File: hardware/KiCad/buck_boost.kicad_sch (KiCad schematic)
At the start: 51 parts, among them Q1 BSC030N08NS5, Q2 BSC030N08NS5, Q3 BSC030N08NS5, Q4 BSC030N08NS5, U2 CC6937S8-3FB020, U3 CC6937S8-3FB020

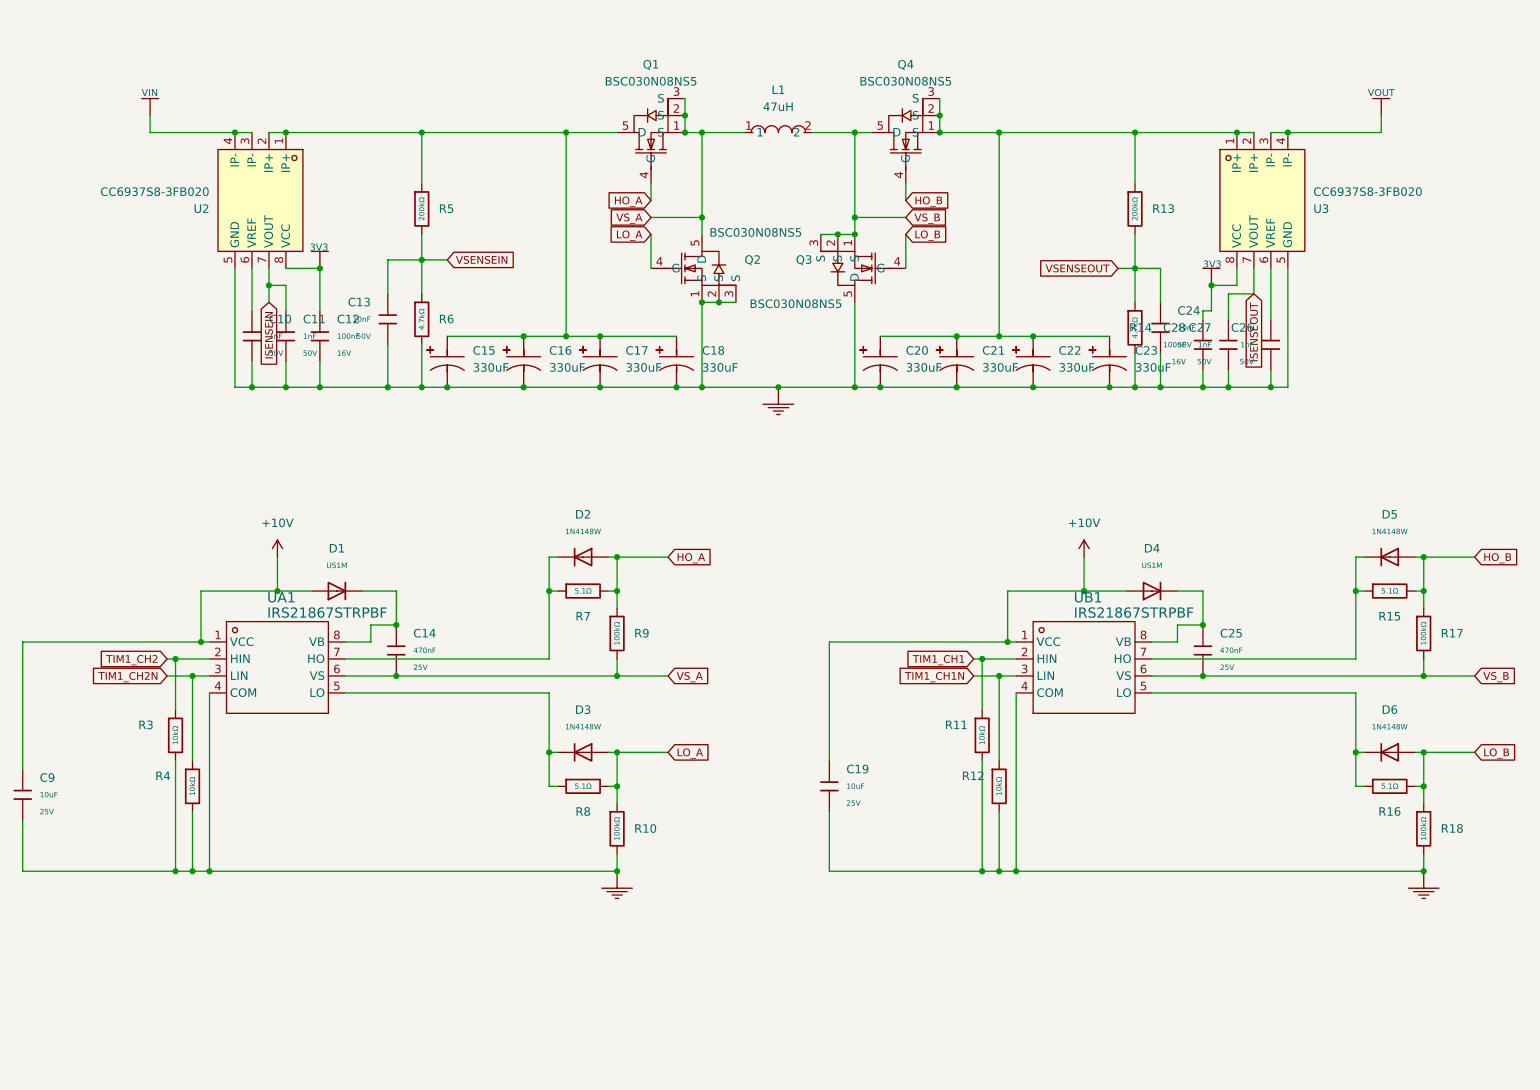
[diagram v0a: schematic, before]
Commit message: Vendor easyeda2kicad component library; rename project files; fix stale part data
Vendors the 16 easyeda2kicad:* parts (symbols/footprints/3D models) that
were referenced but never committed, registers them in sym-lib-table and
a new fp-lib-table, and adds the EASYEDA2KICAD project text variable so
existing 3D-model paths resolve.

Also corrects BSC030N08NS5's stale metadata (was pointing at an ElecSuper
clone, C49108769, instead of the genuine Infineon part, C501507) and
swaps its footprint to the freshly-fetched one, and fixes STANDARDS.md's
Hardware Universe table (stale reference designators, stale MOSFET/
CC6937 LCSC numbers, ~13 previously undocumented parts, wrong library
path).

Renames the auto-generated project/sheet filenames to something legible:
ProPrj_STM32 MPPT_2024-07-25_15-40-35_2026-05-30.* -> openMPPT_v1.3.*,
and the numbered "N_Name Stuff.kicad_sch" sheets -> mcu/buck_boost/
connectors.kicad_sch. Verified via kicad-cli ERC/DRC before and after -
same violation counts, no structural breakage.

Co-Authored-By: Claude Sonnet 5 <noreply@anthropic.com>
Claude-Session: https://claude.ai/code/session_01FKwww6crXDCSrRUFRETJEs
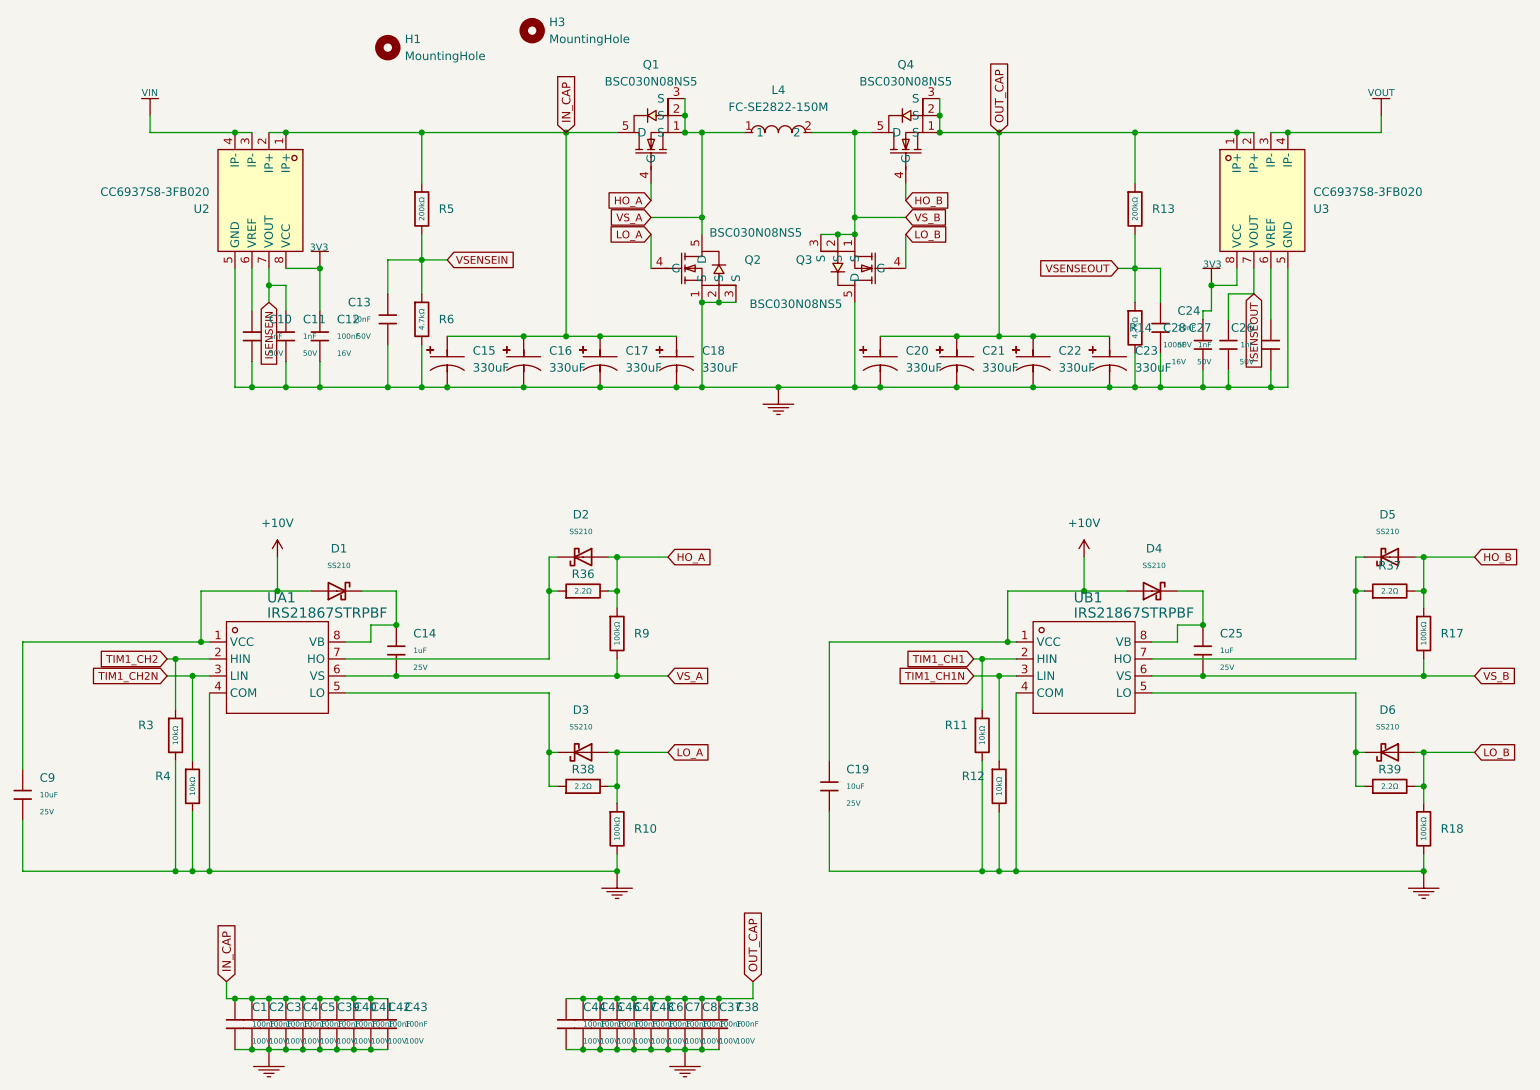
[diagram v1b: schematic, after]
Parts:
- removed C14, C25: 470nF, PCM_JLCPCB:C_0603, symbol JLCPCB-Capacitors:0603,470nF
- removed D1, D4: US1M, PCM_JLCPCB:D_SMA, symbol JLCPCB-Diodes:Recovery,US1M
- removed D2, D3, D5, D6: 1N4148W, PCM_JLCPCB:D_SOD-123, symbol JLCPCB-Diodes:Switching,1N4148W,(2)
- removed L1: 47uH, easyeda2kicad:IND-TH_L32.2-W22.2_CPEX3222L, symbol easyeda2kicad:CPEX3222L-470MC-RS
- removed R15, R16, R7, R8: 5.1Ω, PCM_JLCPCB:R_0603, symbol JLCPCB-Resistors:0603,5.1Ω
- added C1, C2, C3, C37, C38, C39, C4, C40, C41, C42, C43, C44, C45, C46, C47, C48, C5, C6, C7, C8: 100nF, PCM_JLCPCB:C_0805, symbol JLCPCB-Capacitors:0805,100nF
- added C14, C25: 1uF, PCM_JLCPCB:C_0402, symbol JLCPCB-Capacitors:0402,1uF
- added D1, D2, D3, D4, D5, D6: SS210, PCM_JLCPCB:D_SMA, symbol JLCPCB-Diodes:Schottky,SS210
- added H1, H3: MountingHole, MountingHole:MountingHole_3.2mm_M3_DIN965, symbol Mechanical:MountingHole
- added L4: FC-SE2822-150M, easyeda2kicad:IND-TH_L28.0-W23.0_FC-SE2822, symbol easyeda2kicad:FC-SE2822-150M
- added R36, R37, R38, R39: 2.2Ω, PCM_JLCPCB:R_0603, symbol JLCPCB-Resistors:0603,2.2Ω
- Q1, Q2, Q3, Q4: footprint easyeda2kicad:TDSON-8_L5.9-W5.2-P1.27-BL-1 -> easyeda2kicad:PG-TDSON-8_L5.0-W6.0-P1.27-BL-EP; LCSC Part C49108769 -> C501507; MPN BSC030N08NS5(ES) -> BSC030N08NS5; Manufacturer ElecSuper(静芯) -> Infineon
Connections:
- net +10V: now also D1.2, D4.2
- net GND: now also C1.2, C2.2, C3.2, C37.2, C38.2, C39.2, C4.2, C40.2, C41.2, C42.2, C43.2, C44.2, C45.2, C46.2, C47.2, C48.2, C5.2, C6.2, C7.2, C8.2
- net HO_A: now also D2.2, R36.2
- net HO_B: now also D5.2, R37.2
- net LO_A: now also D3.2, R38.2
- net LO_B: now also D6.2, R39.2
- net VS_A: now also C14.2, L4.1
- net VS_B: now also C25.2, L4.2
- net IN_CAP: now reaches C15.1 (+), C16.1 (+), C17.1 (+), C18.1 (+), Q1.5 (D), R5.1, U2.1 (IP+), U2.2 (IP+)
- net IN_CAP: now also C1.1, C2.1, C3.1, C39.1, C4.1, C40.1, C41.1, C42.1, C43.1, C5.1
- net at UA1.7 (HO): now also D2.1, R36.1
- net at UA1.5 (LO): now also D3.1, R38.1
- net at UB1.5 (LO): now also D6.1, R39.1
- net at UA1.8 (VB): now also C14.1, D1.1
- net OUT_CAP: now reaches C20.1 (+), C21.1 (+), C22.1 (+), C23.1 (+), Q4.1 (S), Q4.2 (S), Q4.3 (S), R13.1, U3.1 (IP+), U3.2 (IP+)
- net OUT_CAP: now also C37.1, C38.1, C44.1, C45.1, C46.1, C47.1, C48.1, C6.1, C7.1, C8.1
- net at UB1.7 (HO): now also D5.1, R37.1
- net at UB1.8 (VB): now also C25.1, D4.1

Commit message: fix: correct diode part data, select L4 inductor, drop DRC/ERC mandate
Diode inventory (D1-D7): replaced STANDARDS.md's fictional D_BOOT (US1M)
and D_OFF (1N4148W) rows - never actually placed - with the real,
schematic-verified parts: SS210 for both the gate-driver bootstrap role
(D1/D4) and gate-discharge role (D2/D3/D5/D6), and SS510 as the SCT2A25
switch-node freewheeling diode (D7). Fixes the PCB footprint mismatch on
D2/D3/D5/D6 (D_SOD-123 -> D_SMA, matching what the schematic already
specified and SS210 actually needs) and the JLCPCB/PCM_JLCPCB library
nickname mismatch on UA1/UB1's footprint reference.

L4 main inductor: replaced FC-SE2822-150M with HCZH-3218-150-M (C53699952)
in the schematic - same 15uH, lower DCR (3.5mOhm -> 2.2mOhm, cutting
conduction loss from 1.40W to 0.88W) for a $1.56 premium. Chosen after
evaluating and rejecting a higher-margin option (RSEQ32-220M) that cost
2.7x more and had far less stock for headroom this design doesn't need.
Full reasoning and rejected alternatives documented in CALCULATIONS.typ
Section 8. PCB footprint not yet updated for L4 (different pad format,
needs a deliberate swap, not a drop-in edit).

DRC/ERC: removed the "Claude runs kicad-cli DRC/ERC" mandate from
STANDARDS.md - board correctness review is the user's job, not something
to check automatically or by default.

Co-Authored-By: Claude Sonnet 5 <noreply@anthropic.com>
Claude-Session: https://claude.ai/code/session_01FKwww6crXDCSrRUFRETJEs
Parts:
- L4: value FC-SE2822-150M -> HCZH-3218-150-M; footprint easyeda2kicad:IND-TH_L28.0-W23.0_FC-SE2822 -> easyeda2kicad:IND-TH_L33.5-W23.0-P12.00_HCZH-3218; symbol easyeda2kicad:FC-SE2822-150M -> easyeda2kicad:HCZH-3218-150-M; LCSC Part C46553544 -> C53699952; MPN FC-SE2822-150M -> HCZH-3218-150-M; Manufacturer FC(方成) -> YOUCHI(佑驰)
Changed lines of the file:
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@@
 	)
 	(symbol
-		(lib_id "easyeda2kicad:FC-SE2822-150M")
+		(lib_id "easyeda2kicad:HCZH-3218-150-M")
 		(at 144.78 43.18 0)
 		(unit 1)
@@
 			)
 		)
-		(property "Value" "FC-SE2822-150M"
+		(property "Value" "HCZH-3218-150-M"
 			(at 144.78 39.37 0)
 			(show_name no)
@@
 			)
 		)
-		(property "Footprint" "easyeda2kicad:IND-TH_L28.0-W23.0_FC-SE2822"
+		(property "Footprint" "easyeda2kicad:IND-TH_L33.5-W23.0-P12.00_HCZH-3218"
 			(at 144.78 50.8 0)
 			(hide yes)
@@
 			)
 		)
-		(property "Datasheet" "https://www.lcsc.com/datasheet/C46553544.pdf"
+		(property "Datasheet" "https://www.lcsc.com/datasheet/C53699952.pdf"
 			(at 144.78 53.34 0)
 			(hide yes)
@@
 			)
 		)
-		(property "Manufacturer" "FC(方成)"
+		(property "Manufacturer" "YOUCHI(佑驰)"
 			(at 144.78 55.88 0)
 			(hide yes)
@@
 			)
 		)
-		(property "MPN" "FC-SE2822-150M"
+		(property "MPN" "HCZH-3218-150-M"
 			(at 144.78 58.42 0)
 			(hide yes)
@@
 			)
 		)
-		(property "LCSC Part" "C46553544"
+		(property "LCSC Part" "C53699952"
 			(at 144.78 60.96 0)
 			(hide yes)
